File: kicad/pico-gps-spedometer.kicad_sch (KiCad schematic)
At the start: 24 parts, among them J1 Akkumulátor be, J2 TP4056-18650-Charger, J3 uBlox NEO GPS (6M/8M), Q1 PN2222A, Q2 BC212, U1 RP2040-ZERO, U2 DS18B20, U3 LM7805_TO220, U4 TFT_320x240

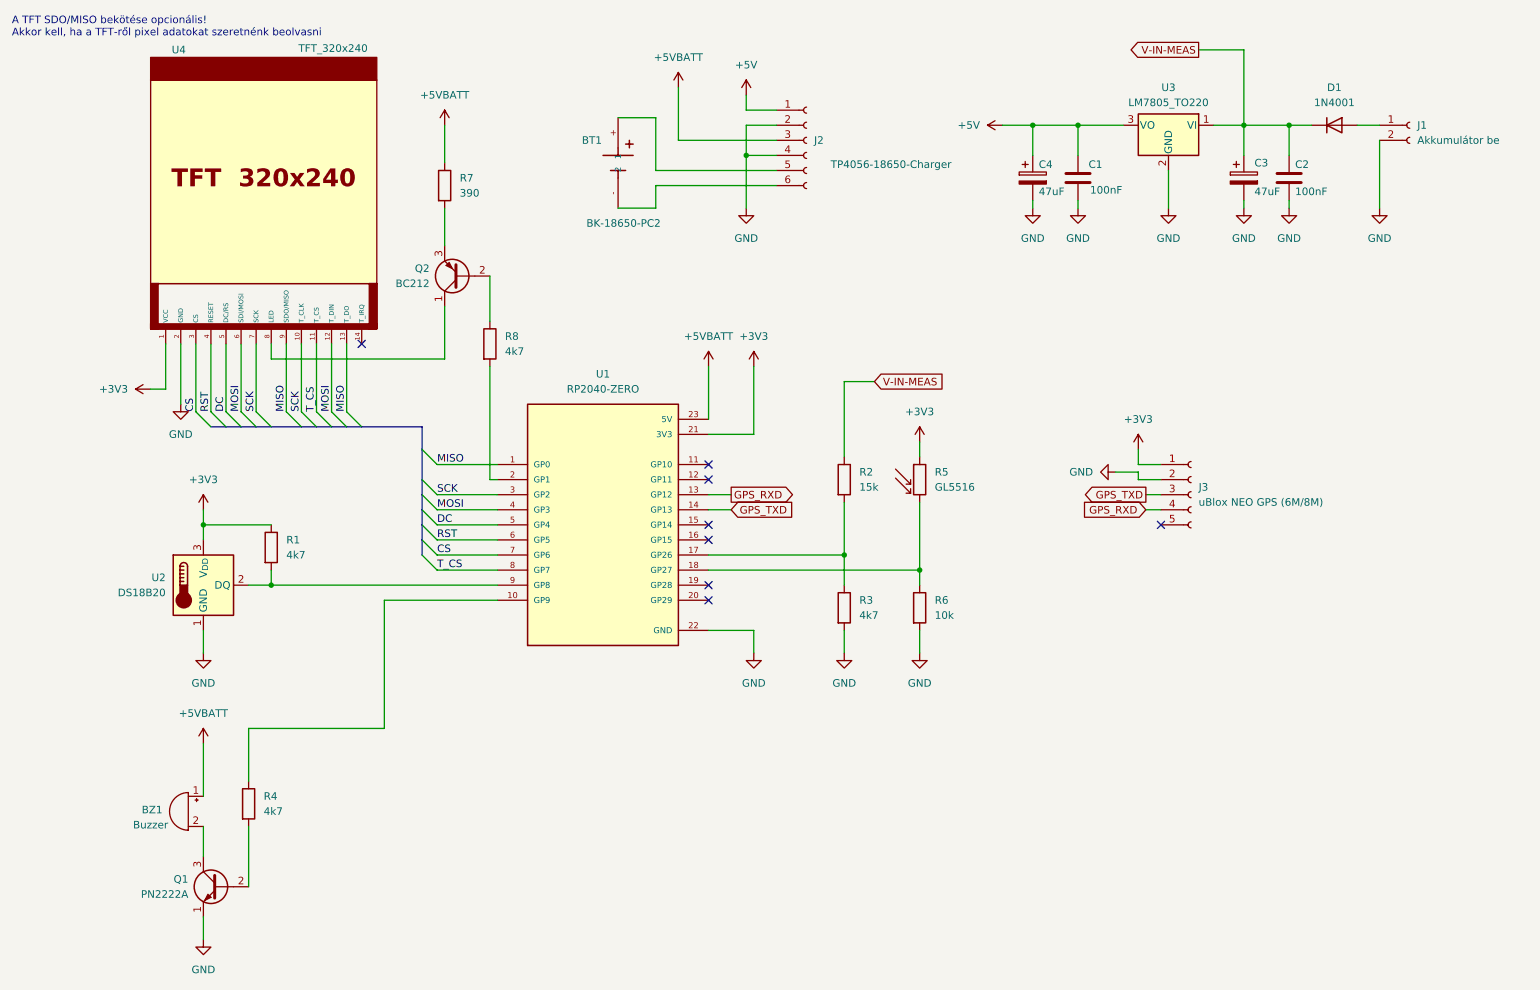
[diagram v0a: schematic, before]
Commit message: Refactor power net naming and update schematic properties
- Changed net name from "+5VBATT" to "+BATT" in PCB and schematic files for consistency.
- Updated various properties in the schematic to reflect the new net name.
- Adjusted positions of certain properties for better alignment and readability.
- Corrected the spelling of "Speedometer" in the PCB file.
- Modified resistor value from "22k" to "15k" in the PCB file.
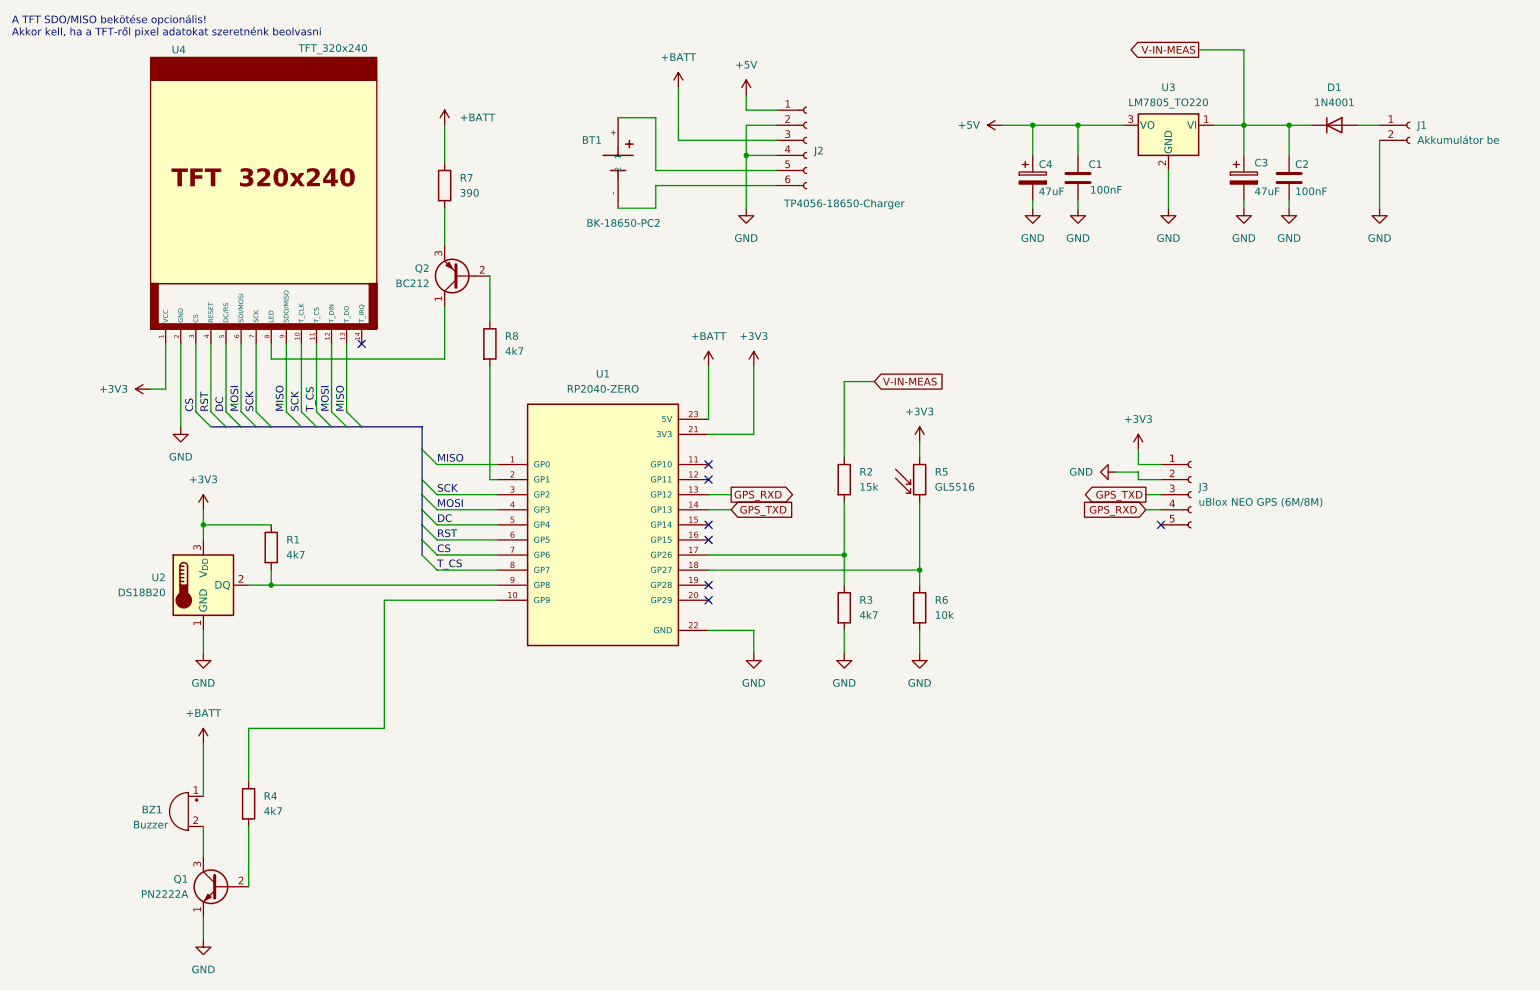
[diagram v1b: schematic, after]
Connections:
- net +5VBATT renamed +BATT
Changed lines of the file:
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@@
 	(wire
 		(pts
-			(xy 43.18 68.58) (xy 43.18 78.74)
+			(xy 43.18 68.58) (xy 43.18 82.55)
 		)
 		(stroke
@@
 			)
 		)
-		(property "Value" "+5VBATT"
-			(at 87.63 26.67 0)
+		(property "Value" "+BATT"
+			(at 90.17 30.4799 0)
 			(effects
 				(font
 					(size 1.27 1.27)
 				)
+				(justify left)
 			)
 		)
@@
 		(dnp no)
 		(property "Reference" "J2"
-			(at 149.86 34.2899 0)
+			(at 149.86 36.068 0)
 			(effects
 				(font
@@
 		)
 		(property "Value" "TP4056-18650-Charger"
-			(at 152.654 38.354 0)
+			(at 144.78 44.958 0)
 			(effects
 				(font
@@
 	(symbol
 		(lib_id "power:GND")
-		(at 43.18 78.74 0)
+		(at 43.18 82.55 0)
 		(unit 1)
 		(exclude_from_sim no)
@@
 		(fields_autoplaced yes)
 		(property "Reference" "#PWR04"
-			(at 43.18 85.09 0)
+			(at 43.18 88.9 0)
 			(effects
 				(font
@@
 		)
 		(property "Value" "GND"
-			(at 43.18 83.82 0)
+			(at 43.18 87.63 0)
 			(effects
 				(font
@@
 		)
 		(property "Footprint" ""
-			(at 43.18 78.74 0)
+			(at 43.18 82.55 0)
 			(effects
 				(font
@@
 		)
 		(property "Datasheet" ""
-			(at 43.18 78.74 0)
+			(at 43.18 82.55 0)
 			(effects
 				(font
@@
 		)
 		(property "Description" "Power symbol creates a global label with name \"GND\" , ground"
-			(at 43.18 78.74 0)
+			(at 43.18 82.55 0)
 			(effects
 				(font
@@
 			)
 		)
-		(property "Value" "+5VBATT"
+		(property "Value" "+BATT"
 			(at 132.08 67.31 0)
 			(effects
@@
 			)
 		)
-		(property "Value" "+5VBATT"
+		(property "Value" "+BATT"
 			(at 127 20.32 0)
 			(effects
@@
 			)
 		)
-		(property "Value" "+5VBATT"
+		(property "Value" "+BATT"
 			(at 46.99 130.81 0)
 			(effects
